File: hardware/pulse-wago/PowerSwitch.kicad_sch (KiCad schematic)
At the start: 22 parts, among them J1801 Conn_01x01, J1802 Conn_01x01, U1801 BTT6010

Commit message: Update library
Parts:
- C1801: footprint Capacitor_SMD:C_1210_3225Metric -> V2_Capacitor_SMD:C_1210; symbol Device:C_Small -> V2_Device:C_1210_10u; Manufacturer (none) -> TDK; Mouser (none) -> 810-CNA6P1X7R1H106K2; Product (none) -> CNA6P1X7R1H106K250AE; Rating (none) -> 50V
- C1802, C1803, C1804, C1805, C1806, C1807: footprint Capacitor_SMD:C_0603_1608Metric -> V2_Capacitor_SMD:C_0603; symbol Device:C_Small -> V2_Device:C_0603_0u1; Manufacturer (none) -> TDK; Mouser (none) -> 810-CGA3E2X7R1H104MA; Product (none) -> CGA3E2X7R1H104M080AA; Rating (none) -> 50V
- D1801: footprint Diode_SMD:D_SOD-523 -> V2_Diode_SMD:D_SOD-523; Manufacturer (none) -> ROHM Semiconductor; Mouser (none) -> 755-RB501SM-30FHT2R; Product (none) -> RB501SM-30FHT2R
- J1801, J1802: value Conn_01x01 -> WAGO 2065-100; Manufacturer (none) -> WAGO; Product (none) -> 2065-100/998-403
- R1801, R1804, R1806: footprint Resistor_SMD:R_0603_1608Metric -> V2_Resistor_SMD:R_0603; symbol Device:R_Small -> V2_Device:R_0603_100k; Manufacturer (none) -> Vishay; Mouser (none) -> 71-CRCW0603100KFKEAC; Product (none) -> CRCW0603100KFKEAC; Rating (none) -> 100mW
- R1802, R1803, R1807, R1808: footprint Resistor_SMD:R_0603_1608Metric -> V2_Resistor_SMD:R_0603; symbol Device:R_Small -> V2_Device:R_0603_10k; Manufacturer (none) -> Vishay; Mouser (none) -> 71-CRCW060310K0FKEAC; Product (none) -> CRCW060310K0FKEAC; Rating (none) -> 100mW
- R1805: footprint Resistor_SMD:R_0603_1608Metric -> V2_Resistor_SMD:R_0603; symbol Device:R_Small -> V2_Device:R_0603_100R; Manufacturer (none) -> Vishay; Mouser (none) -> 71-CRCW0603100RFKEAH; Product (none) -> CRCW0603100RFKEAHP; Rating (none) -> 330mW
- R1809, R1810: footprint Resistor_SMD:R_0603_1608Metric -> V2_Resistor_SMD:R_0603; symbol Device:R_Small -> V2_Device:R_0603_2k7; Manufacturer (none) -> Vishay; Mouser (none) -> 71-CRCW06032K70FKEAC; Product (none) -> CRCW06032K70FKEAC; Rating (none) -> 100mW
- TVS1801: value SMAJ36CA -> SMBJ33CA; footprint Diode_SMD:D_SMA -> V2_Diode_SMD:D_SMB; symbol V2_Diode:SMAJ36CA -> V2_Diode:SMBJ33CA; Manufacturer (none) -> Bourns; Mouser (none) -> 652-SMBJ33CA-Q; Product (none) -> SMBJ33CA-Q; Rating (none) -> 33V
- U1801: Manufacturer (none) -> Infineon; Mouser (none) -> 726-BTT60101ERBXUMA1; Product (none) -> BTT60101ERBXUMA1
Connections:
- net +24V renamed +28V
- net +24V-Supply renamed +28V-Supply
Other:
- note added: "100R / Solenoid coil voltage divider Supplies reference voltage to a single channel while the +28V power is switched off."
- note removed: "100R / Solenoid coil voltage divider Supplies reference voltage to a single channel while the +24V power is switched off."
- moved on the sheet: C1801, C1802, C1806, D1801, J1801, J1802, R1805, TVS1801

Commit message: Update Library
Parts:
- C1801: symbol V2_Device:C_1210_10u -> V2_Capacitor:1210_10u
- C1802, C1803, C1804, C1805, C1806, C1807: symbol V2_Device:C_0603_0u1 -> V2_Capacitor:0603_0u1
- R1801, R1804, R1806: symbol V2_Device:R_0603_100k -> V2_Resistor:0603_100k
- R1802, R1803, R1807, R1808: symbol V2_Device:R_0603_10k -> V2_Resistor:0603_10k
- R1805: symbol V2_Device:R_0603_100R -> V2_Resistor:0603_100R
- R1809, R1810: symbol V2_Device:R_0603_2k7 -> V2_Resistor:0603_2k7
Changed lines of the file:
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@@
 		(on_board yes)
 		(dnp no)
-		(property "Reference" "#PWR01805"
+		(property "Reference" "#PWR1805"
 			(at 118.11 90.17 0)
 			(effects
@@
 			(project "pulse"
 				(path "/6c8448b4-b04d-47e1-934e-e40cbe27a7be/ba748654-beb9-4861-aa35-c19e08caaf2e"
-					(reference "#PWR01805")
+					(reference "#PWR1805")
 					(unit 1)
 				)
@@
 		(on_board yes)
 		(dnp no)
-		(property "Reference" "#PWR01804"
+		(property "Reference" "#PWR1804"
 			(at 218.44 87.63 0)
 			(effects
@@
 			(project "pulse"
 				(path "/6c8448b4-b04d-47e1-934e-e40cbe27a7be/ba748654-beb9-4861-aa35-c19e08caaf2e"
-					(reference "#PWR01804")
+					(reference "#PWR1804")
 					(unit 1)
 				)
@@
 	)
 	(symbol
-		(lib_id "V2_Device:C_1210_10u")
+		(lib_id "V2_Capacitor:1210_10u")
 		(at 135.89 78.74 0)
 		(unit 1)
@@
 	)
 	(symbol
-		(lib_id "V2_Device:R_0603_10k")
+		(lib_id "V2_Resistor:0603_10k")
 		(at 99.06 125.73 270)
 		(unit 1)
@@
 		(on_board yes)
 		(dnp no)
-		(property "Reference" "#PWR01802"
+		(property "Reference" "#PWR1802"
 			(at 147.32 87.63 0)
 			(effects
@@
 			(project "pulse"
 				(path "/6c8448b4-b04d-47e1-934e-e40cbe27a7be/ba748654-beb9-4861-aa35-c19e08caaf2e"
-					(reference "#PWR01802")
+					(reference "#PWR1802")
 					(unit 1)
 				)
@@
 	)
 	(symbol
-		(lib_id "V2_Device:R_0603_10k")
+		(lib_id "V2_Resistor:0603_10k")
 		(at 91.44 135.89 90)
 		(unit 1)
@@
 		(on_board yes)
 		(dnp no)
-		(property "Reference" "#PWR01817"
+		(property "Reference" "#PWR1817"
 			(at 104.14 147.32 0)
 			(effects
@@
 			(project "pulse"
 				(path "/6c8448b4-b04d-47e1-934e-e40cbe27a7be/ba748654-beb9-4861-aa35-c19e08caaf2e"
-					(reference "#PWR01817")
+					(reference "#PWR1817")
 					(unit 1)
 				)
@@
 	)
 	(symbol
-		(lib_id "V2_Device:R_0603_10k")
+		(lib_id "V2_Resistor:0603_10k")
 		(at 208.28 76.2 90)
 		(unit 1)
@@
 		(on_board yes)
 		(dnp no)
-		(property "Reference" "#PWR01810"
+		(property "Reference" "#PWR1810"
 			(at 151.13 132.08 0)
 			(effects
@@
 			(project "pulse"
 				(path "/6c8448b4-b04d-47e1-934e-e40cbe27a7be/ba748654-beb9-4861-aa35-c19e08caaf2e"
-					(reference "#PWR01810")
+					(reference "#PWR1810")
 					(unit 1)
 				)
@@
 		(on_board yes)
 		(dnp no)
-		(property "Reference" "#PWR01807"
+		(property "Reference" "#PWR1807"
 			(at 91.44 120.65 0)
 			(effects
@@
 			(project "pulse"
 				(path "/6c8448b4-b04d-47e1-934e-e40cbe27a7be/ba748654-beb9-4861-aa35-c19e08caaf2e"
-					(reference "#PWR01807")
+					(reference "#PWR1807")
 					(unit 1)
 				)
@@
 	)
 	(symbol
-		(lib_id "V2_Device:R_0603_2k7")
+		(lib_id "V2_Resistor:0603_2k7")
 		(at 104.14 138.43 0)
 		(unit 1)
@@
 		(on_board yes)
 		(dnp no)
-		(property "Reference" "#PWR01814"
+		(property "Reference" "#PWR1814"
 			(at 212.09 137.16 0)
 			(effects
@@
 			(project "pulse"
 				(path "/6c8448b4-b04d-47e1-934e-e40cbe27a7be/ba748654-beb9-4861-aa35-c19e08caaf2e"
-					(reference "#PWR01814")
+					(reference "#PWR1814")
 					(unit 1)
 				)
@@
 		(on_board yes)
 		(dnp no)
-		(property "Reference" "#PWR01806"
+		(property "Reference" "#PWR1806"
 			(at 194.31 121.92 0)
 			(effects
@@
 			(project "pulse"
 				(path "/6c8448b4-b04d-47e1-934e-e40cbe27a7be/ba748654-beb9-4861-aa35-c19e08caaf2e"
-					(reference "#PWR01806")
+					(reference "#PWR1806")
 					(unit 1)
 				)
@@
 	)
 	(symbol
-		(lib_id "V2_Device:R_0603_10k")
+		(lib_id "V2_Resistor:0603_10k")
 		(at 193.04 78.74 0)
 		(unit 1)
@@
 	)
 	(symbol
-		(lib_id "V2_Device:R_0603_100k")
+		(lib_id "V2_Resistor:0603_100k")
 		(at 193.04 71.12 0)
 		(unit 1)
@@
 		(on_board yes)
 		(dnp no)
-		(property "Reference" "#PWR01815"
+		(property "Reference" "#PWR1815"
 			(at 139.7 135.89 0)
 			(effects
@@
 			(project "pulse"
 				(path "/6c8448b4-b04d-47e1-934e-e40cbe27a7be/ba748654-beb9-4861-aa35-c19e08caaf2e"
-					(reference "#PWR01815")
+					(reference "#PWR1815")
 					(unit 1)
 				)
@@
 	)
 	(symbol
-		(lib_id "V2_Device:C_0603_0u1")
+		(lib_id "V2_Capacitor:0603_0u1")
 		(at 151.13 123.19 0)
 		(unit 1)
@@
 		(on_board yes)
 		(dnp no)
-		(property "Reference" "#PWR01801"
+		(property "Reference" "#PWR1801"
 			(at 135.89 87.63 0)
 			(effects
@@
 			(project "pulse"
 				(path "/6c8448b4-b04d-47e1-934e-e40cbe27a7be/ba748654-beb9-4861-aa35-c19e08caaf2e"
-					(reference "#PWR01801")
+					(reference "#PWR1801")
 					(unit 1)
 				)
@@
 		(on_board yes)
 		(dnp no)
-		(property "Reference" "#PWR01808"
+		(property "Reference" "#PWR1808"
 			(at 163.83 124.46 0)
 			(effects
@@
 			(project "pulse"
 				(path "/6c8448b4-b04d-47e1-934e-e40cbe27a7be/ba748654-beb9-4861-aa35-c19e08caaf2e"
-					(reference "#PWR01808")
+					(reference "#PWR1808")
 					(unit 1)
 				)
@@
 	)
 	(symbol
-		(lib_id "V2_Device:R_0603_100k")
+		(lib_id "V2_Resistor:0603_100k")
 		(at 82.55 120.65 270)
 		(unit 1)
@@
 	)
 	(symbol
-		(lib_id "V2_Device:R_0603_100k")
+		(lib_id "V2_Resistor:0603_100k")
 		(at 138.43 123.19 0)
 		(unit 1)
@@
 		(on_board yes)
 		(dnp no)
-		(property "Reference" "#PWR01813"
+		(property "Reference" "#PWR1813"
 			(at 194.31 127 0)
 			(effects
@@
 			(project "pulse"
 				(path "/6c8448b4-b04d-47e1-934e-e40cbe27a7be/ba748654-beb9-4861-aa35-c19e08caaf2e"
-					(reference "#PWR01813")
+					(reference "#PWR1813")
 					(unit 1)
 				)
@@
 	)
 	(symbol
-		(lib_id "V2_Device:R_0603_100R")
+		(lib_id "V2_Resistor:0603_100R")
 		(at 194.31 120.65 0)
 		(unit 1)
@@
 		(on_board yes)
 		(dnp no)
-		(property "Reference" "#PWR01818"
+		(property "Reference" "#PWR1818"
 			(at 113.03 147.32 0)
 			(effects
@@
 			(project "pulse"
 				(path "/6c8448b4-b04d-47e1-934e-e40cbe27a7be/ba748654-beb9-4861-aa35-c19e08caaf2e"
-					(reference "#PWR01818")
+					(reference "#PWR1818")
 					(unit 1)
 				)
@@
 	)
 	(symbol
-		(lib_id "V2_Device:C_0603_0u1")
+		(lib_id "V2_Capacitor:0603_0u1")
 		(at 147.32 78.74 0)
 		(unit 1)
@@
 		(on_board yes)
 		(dnp no)
-		(property "Reference" "#PWR01803"
+		(property "Reference" "#PWR1803"
 			(at 193.04 87.63 0)
 			(effects
@@
 			(project "pulse"
 				(path "/6c8448b4-b04d-47e1-934e-e40cbe27a7be/ba748654-beb9-4861-aa35-c19e08caaf2e"
-					(reference "#PWR01803")
+					(reference "#PWR1803")
 					(unit 1)
 				)
@@
 		(on_board yes)
 		(dnp no)
-		(property "Reference" "#PWR01811"
+		(property "Reference" "#PWR1811"
 			(at 163.83 132.08 0)
 			(effects
@@
 			(project "pulse"
 				(path "/6c8448b4-b04d-47e1-934e-e40cbe27a7be/ba748654-beb9-4861-aa35-c19e08caaf2e"
-					(reference "#PWR01811")
+					(reference "#PWR1811")
 					(unit 1)
 				)
@@
 		(on_board yes)
 		(dnp no)
-		(property "Reference" "#FLG01801"
+		(property "Reference" "#FLG1801"
 			(at 102.87 65.405 0)
 			(effects
@@
 			(project "pulse"
 				(path "/6c8448b4-b04d-47e1-934e-e40cbe27a7be/ba748654-beb9-4861-aa35-c19e08caaf2e"
-					(reference "#FLG01801")
+					(reference "#FLG1801")
 					(unit 1)
 				)
@@
 	)
 	(symbol
-		(lib_id "V2_Device:R_0603_2k7")
+		(lib_id "V2_Resistor:0603_2k7")
 		(at 113.03 138.43 0)
 		(unit 1)
@@
 		(on_board yes)
 		(dnp no)
-		(property "Reference" "#PWR01809"
+		(property "Reference" "#PWR1809"
 			(at 138.43 132.08 0)
 			(effects
@@
 			(project "pulse"
 				(path "/6c8448b4-b04d-47e1-934e-e40cbe27a7be/ba748654-beb9-4861-aa35-c19e08caaf2e"
-					(reference "#PWR01809")
+					(reference "#PWR1809")
 					(unit 1)
 				)
@@
 	)
 	(symbol
-		(lib_id "V2_Device:C_0603_0u1")
+		(lib_id "V2_Capacitor:0603_0u1")
 		(at 85.09 138.43 0)
 		(unit 1)
@@
 		(on_board yes)
 		(dnp no)
-		(property "Reference" "#PWR01816"
+		(property "Reference" "#PWR1816"
 			(at 85.09 147.32 0)
 			(effects
@@
 			(project "pulse"
 				(path "/6c8448b4-b04d-47e1-934e-e40cbe27a7be/ba748654-beb9-4861-aa35-c19e08caaf2e"
-					(reference "#PWR01816")
+					(reference "#PWR1816")
 					(unit 1)
 				)
@@
 	)
 	(symbol
-		(lib_id "V2_Device:C_0603_0u1")
+		(lib_id "V2_Capacitor:0603_0u1")
 		(at 212.09 128.27 0)
 		(unit 1)
@@
 	)
 	(symbol
-		(lib_id "V2_Device:C_0603_0u1")
+		(lib_id "V2_Capacitor:0603_0u1")
 		(at 163.83 123.19 0)
 		(unit 1)
@@
 	)
 	(symbol
-		(lib_id "V2_Device:C_0603_0u1")
+		(lib_id "V2_Capacitor:0603_0u1")
 		(at 218.44 78.74 0)
 		(unit 1)
@@
 		(on_board yes)
 		(dnp no)
-		(property "Reference" "#PWR01812"
+		(property "Reference" "#PWR1812"
 			(at 116.84 130.81 0)
 			(effects
@@
 			(project "pulse"
 				(path "/6c8448b4-b04d-47e1-934e-e40cbe27a7be/ba748654-beb9-4861-aa35-c19e08caaf2e"
-					(reference "#PWR01812")
+					(reference "#PWR1812")
 					(unit 1)
 				)

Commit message: Refresh
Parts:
- U1801: Rating (none) -> 36V
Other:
- company: +24V -> Versio Duo
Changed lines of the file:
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@@
 	(title_block
 		(title "Power Switch")
-		(date "2023-01-07")
-		(rev "1")
-		(company "+24V")
-		(comment 1 "Voltage + Current Sense")
+		(date "2026-02-24")
+		(rev "2026-02-24")
+		(company "Versio Duo")
+		(comment 1 "+28V")
+		(comment 2 "Voltage + Current Sense")
 	)
 	(text "Supply Voltage"
@@
 			)
 		)
-		(property "Description" "Infineon Smart High Sde Switches PROFET™+ 24V"
+		(property "Description" "Infineon Smart High Side Switches PROFET™+ 24V"
 			(at 123.19 128.27 0)
 			(effects
@@
 			(effects
 				(font
+					(size 1.27 1.27)
+				)
+				(hide yes)
+			)
+		)
+		(property "Rating" "36V"
+			(at 123.19 179.07 0)
+			(effects
+				(font

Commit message: Refresh
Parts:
- C1801: Mouser 810-CNA6P1X7R1H106K2 -> 810-CNC6P1X7R1H106K2; Product CNA6P1X7R1H106K250AE -> CNC6P1X7R1H106K250AE
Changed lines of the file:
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@@
 			)
 		)
-		(property "Mouser" "810-CNA6P1X7R1H106K2"
+		(property "Mouser" "810-CNC6P1X7R1H106K2"
 			(at 135.89 101.6 0)
 			(effects
@@
 			)
 		)
-		(property "Product" "CNA6P1X7R1H106K250AE"
+		(property "Product" "CNC6P1X7R1H106K250AE"
 			(at 135.89 96.52 0)
 			(effects

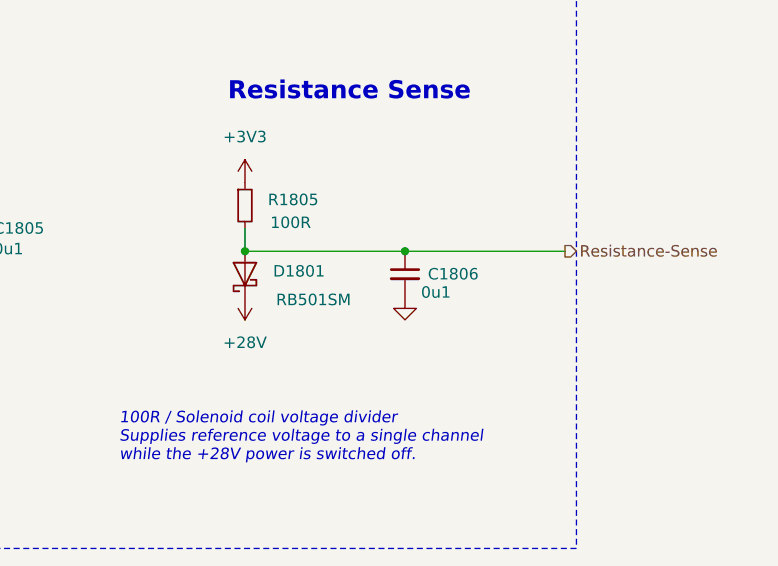
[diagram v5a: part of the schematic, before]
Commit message: Replace diode
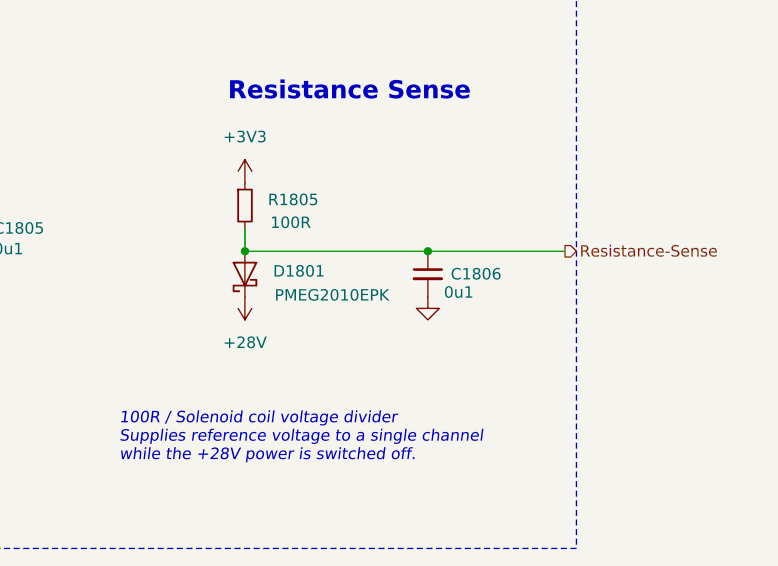
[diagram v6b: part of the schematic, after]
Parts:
- D1801: value RB501SM -> PMEG2010EPK; footprint V2_Diode_SMD:D_SOD-523 -> V2_Diode_SMD:D_SOD-1608; symbol V2_Diode:RB501SM -> V2_Diode:PMEG2010EPK; Manufacturer ROHM Semiconductor -> Nexperia; Mouser 755-RB501SM-30FHT2R -> 771-PMEG2010EPK; Product RB501SM-30FHT2R -> PMEG2010EPK; Rating (none) -> 20V
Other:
- title: Power Switch -> V2 pulse WAGO
- moved on the sheet: C1806

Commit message: Update
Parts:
- C1801: renamed from C1807; Id (none) -> Capacitor:${SYMBOL_NAME}
- C1802: renamed from C1801; Id (none) -> Capacitor:${SYMBOL_NAME}
- C1803: renamed from C1802; Id (none) -> Capacitor:${SYMBOL_NAME}
- C1804, C1805, C1806: Id (none) -> Capacitor:${SYMBOL_NAME}
- C1807: renamed from C1803; Id (none) -> Capacitor:${SYMBOL_NAME}
- D1801, TVS1801: Id (none) -> Diode:${SYMBOL_NAME}
- J1801, J1802: Id (none) -> WAGO:${SYMBOL_NAME}; Rating (none) -> 9A
- R1801: renamed from R1804; Id (none) -> Resistor:${SYMBOL_NAME}
- R1802: renamed from R1808; Id (none) -> Resistor:${SYMBOL_NAME}
- R1803: renamed from R1807; Id (none) -> Resistor:${SYMBOL_NAME}
- R1804: renamed from R1809; Id (none) -> Resistor:${SYMBOL_NAME}
- R1805: renamed from R1810; Id (none) -> Resistor:${SYMBOL_NAME}
- R1806: Id (none) -> Resistor:${SYMBOL_NAME}
- R1807: renamed from R1801; Id (none) -> Resistor:${SYMBOL_NAME}
- R1808: renamed from R1803; Id (none) -> Resistor:${SYMBOL_NAME}
- R1809: renamed from R1805; Id (none) -> Resistor:${SYMBOL_NAME}
- R1810: renamed from R1802; Id (none) -> Resistor:${SYMBOL_NAME}
- U1801: Id (none) -> PowerSwitch:${SYMBOL_NAME}

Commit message: Good Bye Imperial
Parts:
- C1801, C1803, C1804, C1805, C1806, C1807: footprint V2_Capacitor_SMD:C_0603 -> V2_Capacitor_SMD:C_1608; symbol V2_Capacitor:0603_0u1 -> V2_Capacitor:1608_0u1
- C1802: footprint V2_Capacitor_SMD:C_1210 -> V2_Capacitor_SMD:C_3225; symbol V2_Capacitor:1210_10u -> V2_Capacitor:3225_10u
- R1801, R1806, R1807: footprint V2_Resistor_SMD:R_0603 -> V2_Resistor_SMD:R_1608; symbol V2_Resistor:0603_100k -> V2_Resistor:1608_100k
- R1802, R1803, R1808, R1810: footprint V2_Resistor_SMD:R_0603 -> V2_Resistor_SMD:R_1608; symbol V2_Resistor:0603_10k -> V2_Resistor:1608_10k
- R1804, R1805: footprint V2_Resistor_SMD:R_0603 -> V2_Resistor_SMD:R_1608; symbol V2_Resistor:0603_2k7 -> V2_Resistor:1608_2k7
- R1809: footprint V2_Resistor_SMD:R_0603 -> V2_Resistor_SMD:R_1608; symbol V2_Resistor:0603_100R -> V2_Resistor:1608_100R
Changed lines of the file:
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@@
 	)
 	(symbol
-		(lib_id "V2_Capacitor:1210_10u")
+		(lib_id "V2_Capacitor:3225_10u")
 		(at 135.89 78.74 0)
 		(unit 1)
@@
 			)
 		)
-		(property "Footprint" "V2_Capacitor_SMD:C_1210"
+		(property "Footprint" "V2_Capacitor_SMD:C_3225"
 			(at 135.89 95.758 0)
 			(hide yes)
@@
 	)
 	(symbol
-		(lib_id "V2_Resistor:0603_10k")
+		(lib_id "V2_Resistor:1608_10k")
 		(at 99.06 125.73 270)
 		(unit 1)
@@
 			)
 		)
-		(property "Footprint" "V2_Resistor_SMD:R_0603"
+		(property "Footprint" "V2_Resistor_SMD:R_1608"
 			(at 83.312 125.73 0)
 			(hide yes)
@@
 	)
 	(symbol
-		(lib_id "V2_Resistor:0603_10k")
+		(lib_id "V2_Resistor:1608_10k")
 		(at 91.44 135.89 90)
 		(unit 1)
@@
 			)
 		)
-		(property "Footprint" "V2_Resistor_SMD:R_0603"
+		(property "Footprint" "V2_Resistor_SMD:R_1608"
 			(at 107.188 135.89 0)
 			(hide yes)
@@
 	)
 	(symbol
-		(lib_id "V2_Resistor:0603_10k")
+		(lib_id "V2_Resistor:1608_10k")
 		(at 208.28 76.2 90)
 		(unit 1)
@@
 			)
 		)
-		(property "Footprint" "V2_Resistor_SMD:R_0603"
+		(property "Footprint" "V2_Resistor_SMD:R_1608"
 			(at 224.028 76.2 0)
 			(hide yes)
@@
 	)
 	(symbol
-		(lib_id "V2_Resistor:0603_2k7")
+		(lib_id "V2_Resistor:1608_2k7")
 		(at 104.14 138.43 0)
 		(unit 1)
@@
 			)
 		)
-		(property "Footprint" "V2_Resistor_SMD:R_0603"
+		(property "Footprint" "V2_Resistor_SMD:R_1608"
 			(at 104.14 154.178 0)
 			(hide yes)
@@
 	)
 	(symbol
-		(lib_id "V2_Resistor:0603_10k")
+		(lib_id "V2_Resistor:1608_10k")
 		(at 193.04 78.74 0)
 		(unit 1)
@@
 			)
 		)
-		(property "Footprint" "V2_Resistor_SMD:R_0603"
+		(property "Footprint" "V2_Resistor_SMD:R_1608"
 			(at 193.04 94.488 0)
 			(hide yes)
@@
 	)
 	(symbol
-		(lib_id "V2_Resistor:0603_100k")
+		(lib_id "V2_Resistor:1608_100k")
 		(at 193.04 71.12 0)
 		(unit 1)
@@
 			)
 		)
-		(property "Footprint" "V2_Resistor_SMD:R_0603"
+		(property "Footprint" "V2_Resistor_SMD:R_1608"
 			(at 193.04 86.868 0)
 			(hide yes)
@@
 	)
 	(symbol
-		(lib_id "V2_Capacitor:0603_0u1")
+		(lib_id "V2_Capacitor:1608_0u1")
 		(at 151.13 123.19 0)
 		(unit 1)
@@
 			)
 		)
-		(property "Footprint" "V2_Capacitor_SMD:C_0603"
+		(property "Footprint" "V2_Capacitor_SMD:C_1608"
 			(at 151.13 140.208 0)
 			(hide yes)
@@
 	)
 	(symbol
-		(lib_id "V2_Resistor:0603_100k")
+		(lib_id "V2_Resistor:1608_100k")
 		(at 82.55 120.65 270)
 		(unit 1)
@@
 			)
 		)
-		(property "Footprint" "V2_Resistor_SMD:R_0603"
+		(property "Footprint" "V2_Resistor_SMD:R_1608"
 			(at 66.802 120.65 0)
 			(hide yes)
@@
 	)
 	(symbol
-		(lib_id "V2_Resistor:0603_100k")
+		(lib_id "V2_Resistor:1608_100k")
 		(at 138.43 123.19 0)
 		(unit 1)
@@
 			)
 		)
-		(property "Footprint" "V2_Resistor_SMD:R_0603"
+		(property "Footprint" "V2_Resistor_SMD:R_1608"
 			(at 138.43 138.938 0)
 			(hide yes)
@@
 	)
 	(symbol
-		(lib_id "V2_Resistor:0603_100R")
+		(lib_id "V2_Resistor:1608_100R")
 		(at 194.31 120.65 0)
 		(unit 1)
@@
 			)
 		)
-		(property "Footprint" "V2_Resistor_SMD:R_0603"
+		(property "Footprint" "V2_Resistor_SMD:R_1608"
 			(at 194.31 136.398 0)
 			(hide yes)
@@
 	)
 	(symbol
-		(lib_id "V2_Capacitor:0603_0u1")
+		(lib_id "V2_Capacitor:1608_0u1")
 		(at 147.32 78.74 0)
 		(unit 1)
@@
 			)
 		)
-		(property "Footprint" "V2_Capacitor_SMD:C_0603"
+		(property "Footprint" "V2_Capacitor_SMD:C_1608"
 			(at 147.32 95.758 0)
 			(hide yes)
@@
 	)
 	(symbol
-		(lib_id "V2_Resistor:0603_2k7")
+		(lib_id "V2_Resistor:1608_2k7")
 		(at 113.03 138.43 0)
 		(unit 1)
@@
 			)
 		)
-		(property "Footprint" "V2_Resistor_SMD:R_0603"
+		(property "Footprint" "V2_Resistor_SMD:R_1608"
 			(at 113.03 154.178 0)
 			(hide yes)
@@
 	)
 	(symbol
-		(lib_id "V2_Capacitor:0603_0u1")
+		(lib_id "V2_Capacitor:1608_0u1")
 		(at 85.09 138.43 0)
 		(unit 1)
@@
 			)
 		)
-		(property "Footprint" "V2_Capacitor_SMD:C_0603"
+		(property "Footprint" "V2_Capacitor_SMD:C_1608"
 			(at 85.09 155.448 0)
 			(hide yes)
@@
 	)
 	(symbol
-		(lib_id "V2_Capacitor:0603_0u1")
+		(lib_id "V2_Capacitor:1608_0u1")
 		(at 214.63 128.27 0)
 		(unit 1)
@@
 			)
 		)
-		(property "Footprint" "V2_Capacitor_SMD:C_0603"
+		(property "Footprint" "V2_Capacitor_SMD:C_1608"
 			(at 214.63 145.288 0)
 			(hide yes)
@@
 	)
 	(symbol
-		(lib_id "V2_Capacitor:0603_0u1")
+		(lib_id "V2_Capacitor:1608_0u1")
 		(at 163.83 123.19 0)
 		(unit 1)
@@
 			)
 		)
-		(property "Footprint" "V2_Capacitor_SMD:C_0603"
+		(property "Footprint" "V2_Capacitor_SMD:C_1608"
 			(at 163.83 140.208 0)
 			(hide yes)
@@
 	)
 	(symbol
-		(lib_id "V2_Capacitor:0603_0u1")
+		(lib_id "V2_Capacitor:1608_0u1")
 		(at 218.44 78.74 0)
 		(unit 1)
@@
 			)
 		)
-		(property "Footprint" "V2_Capacitor_SMD:C_0603"
+		(property "Footprint" "V2_Capacitor_SMD:C_1608"
 			(at 218.44 95.758 0)
 			(hide yes)
